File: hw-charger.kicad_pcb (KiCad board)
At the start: 4 copper layers, 100 x 65 mm, 164 parts, among them J10 Screw_Terminal_01x02, J17 Conn_01x02, J19 Conn_01x02, J2 Conn_02x04_Odd_Even, J27 Conn_01x05, J3 Screw_Terminal_01x03, J4 Conn_02x05_Odd_Even, J56 Screw_Terminal_01x02, J57 Conn_01x02, J58 Screw_Terminal_01x02, J59 Conn_01x02, J60 Screw_Terminal_01x02, J61 Conn_01x02, J62 Screw_Terminal_01x02, J63 Conn_01x02, J9 Conn_01x02, Q6 BSC0702LS, Q7 BSC0702LS, Q8 BSC0702LS, Q9 BSC0702LS, U1 ME6203A50M3G, U14 Fuse Holder, U15 Fuse Holder, U16 Fuse Holder, U17 Fuse Holder, U2 Jumper Black, U27 BQ25756RRVR, U3 Jumper Black, U72 Jumper Red, U73 Jumper Blue, U74 Fuse 2A, U75 Fuse 2A

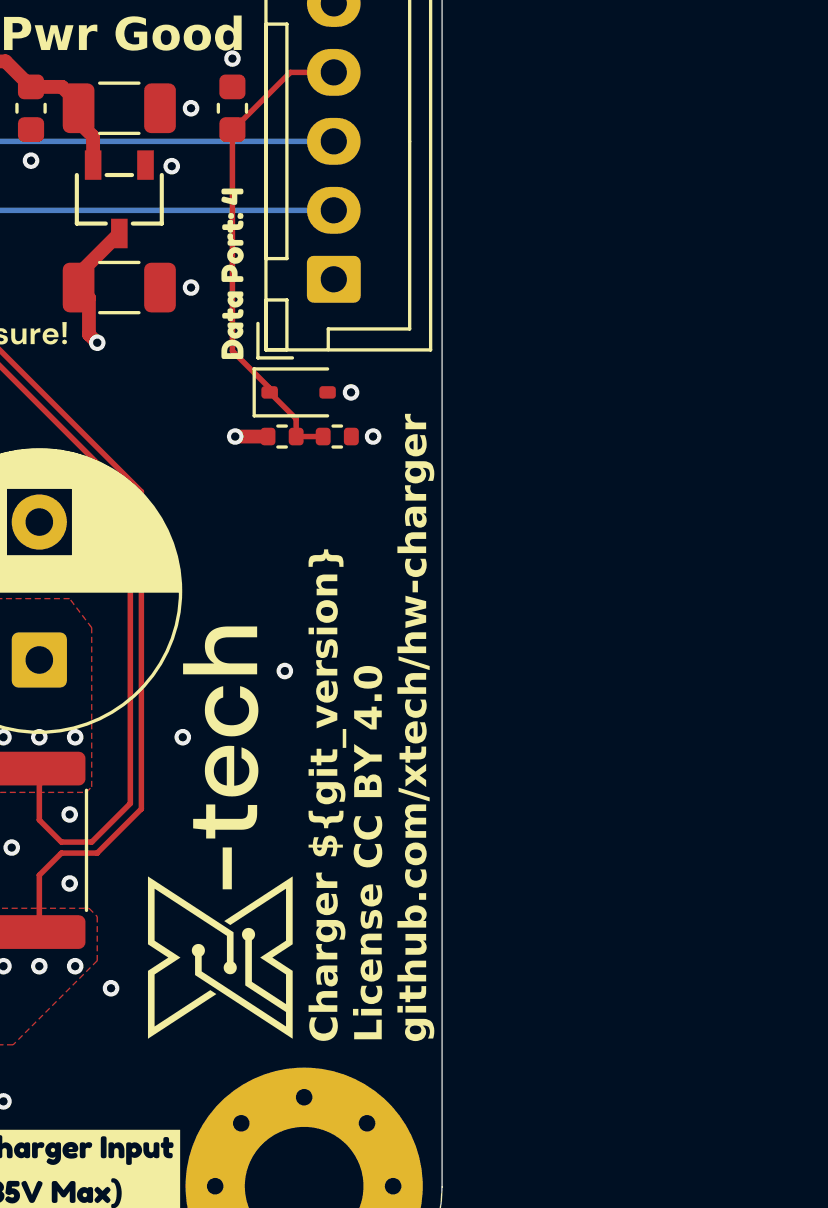
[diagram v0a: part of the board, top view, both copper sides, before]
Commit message: fixed silk screen
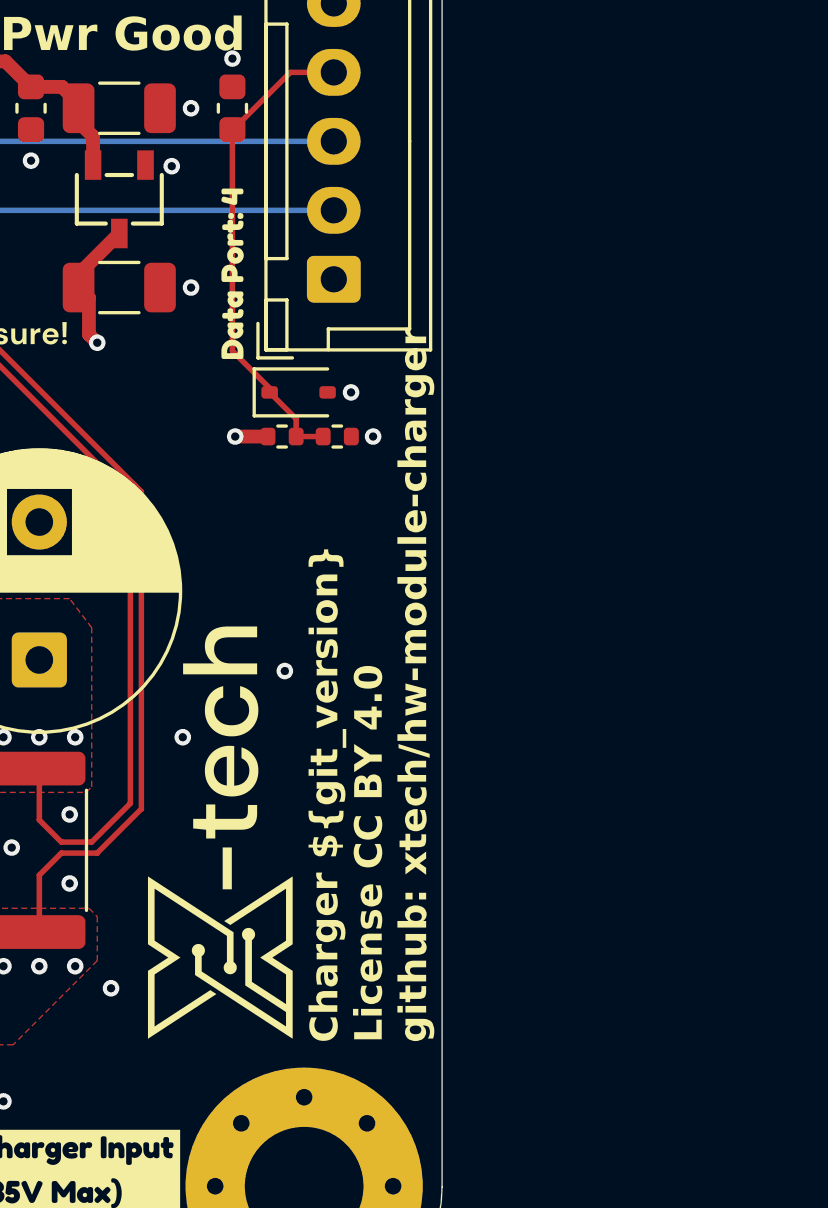
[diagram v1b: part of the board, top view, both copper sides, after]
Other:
- board text added: "Charger ${git_version} License CC BY 4.0 github: xtech/hw-module-charger"
- board text removed: "Charger ${git_version} License CC BY 4.0 github.com/xtech/hw-charger"
